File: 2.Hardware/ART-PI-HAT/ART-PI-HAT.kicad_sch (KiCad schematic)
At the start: 28 parts, among them J1 Conn_02x20_Odd_Even, J2 Conn_02x20_Odd_Even, J3 GC9A01, U1 XC6206_1.8V, U2 MAX30102, U3 MPU-6050, U4 GP-02, U5 IPEX_CONN

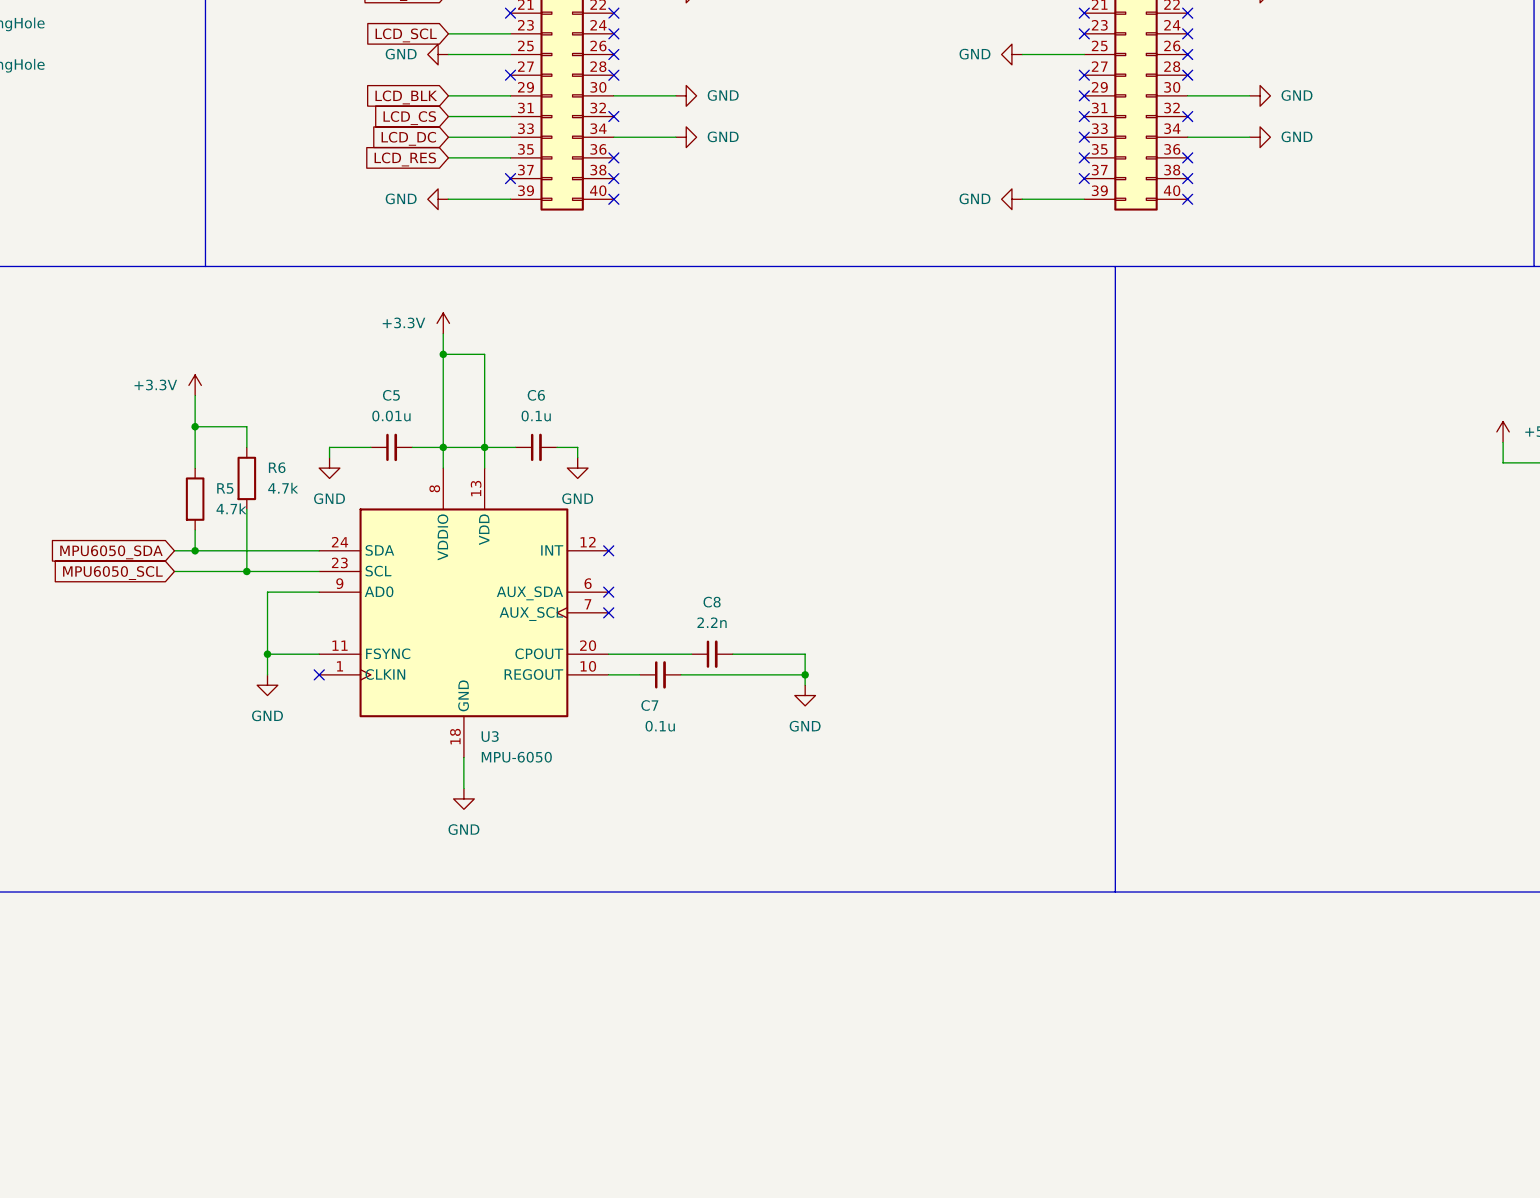
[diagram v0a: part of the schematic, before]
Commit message: add lever switch.
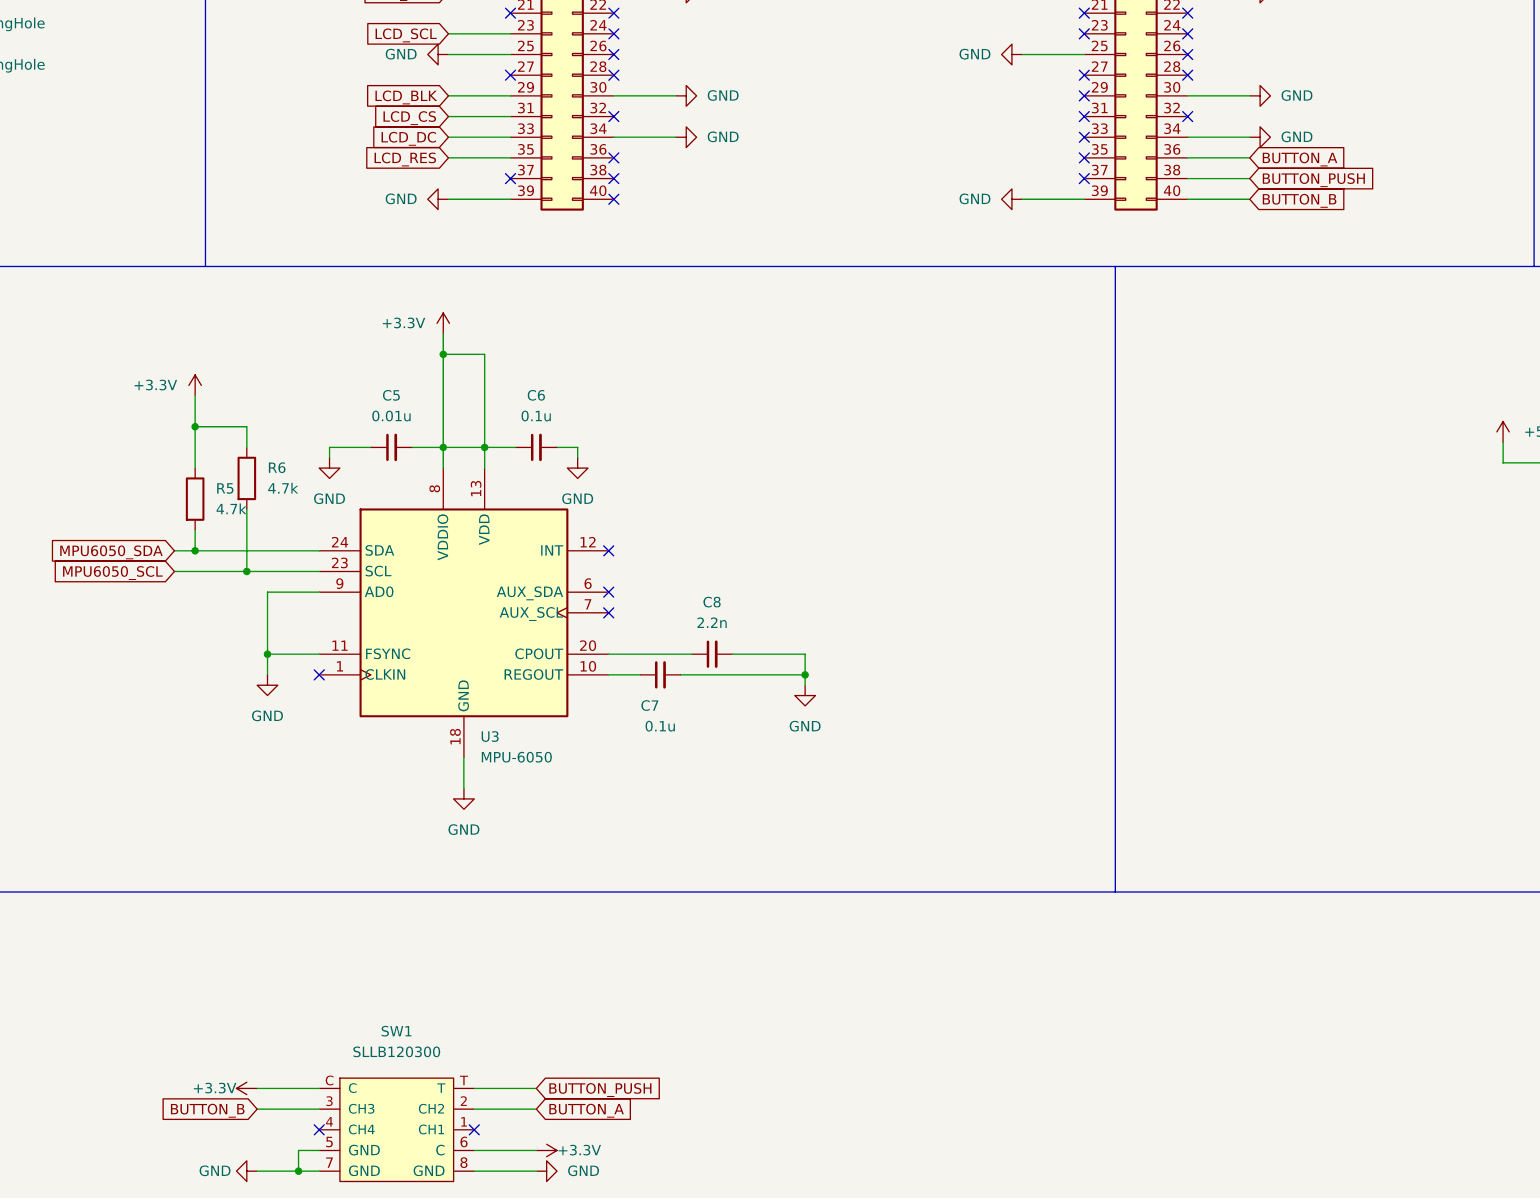
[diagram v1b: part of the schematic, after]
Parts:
- added SW1: SLLB120300, Library:SW-SMD_SLLB120200, symbol SLLB120300:SLLB120300
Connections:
- net +3V3: now also SW1.6 (C), SW1.C
- net GND: now also SW1.5 (GND), SW1.7 (GND), SW1.8 (GND)
- net BUTTON_A: now reaches J2.36 (Pin_36)
- net BUTTON_A: now also SW1.2 (CH2)
- net BUTTON_PUSH: now reaches J2.38 (Pin_38)
- net BUTTON_PUSH: now also SW1.T
- net BUTTON_B: now reaches J2.40 (Pin_40)
- net BUTTON_B: now also SW1.3 (CH3)
- no-connect marks 55 -> 54
